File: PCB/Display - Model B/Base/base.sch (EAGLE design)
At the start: 32 parts, among them J1 SNG-2MM-HEADER-07-V, Q1 MMBT3904, Q2 MMBT3904, Q3 MMBT3904, Q4 MMBT3904, U1 PCA9634PW, U2 TSL2561FN, X1 CLOCK_LED_SEGMENT, X2 CLOCK_LED_SEGMENT, X3 CLOCK_LED_SEGMENT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

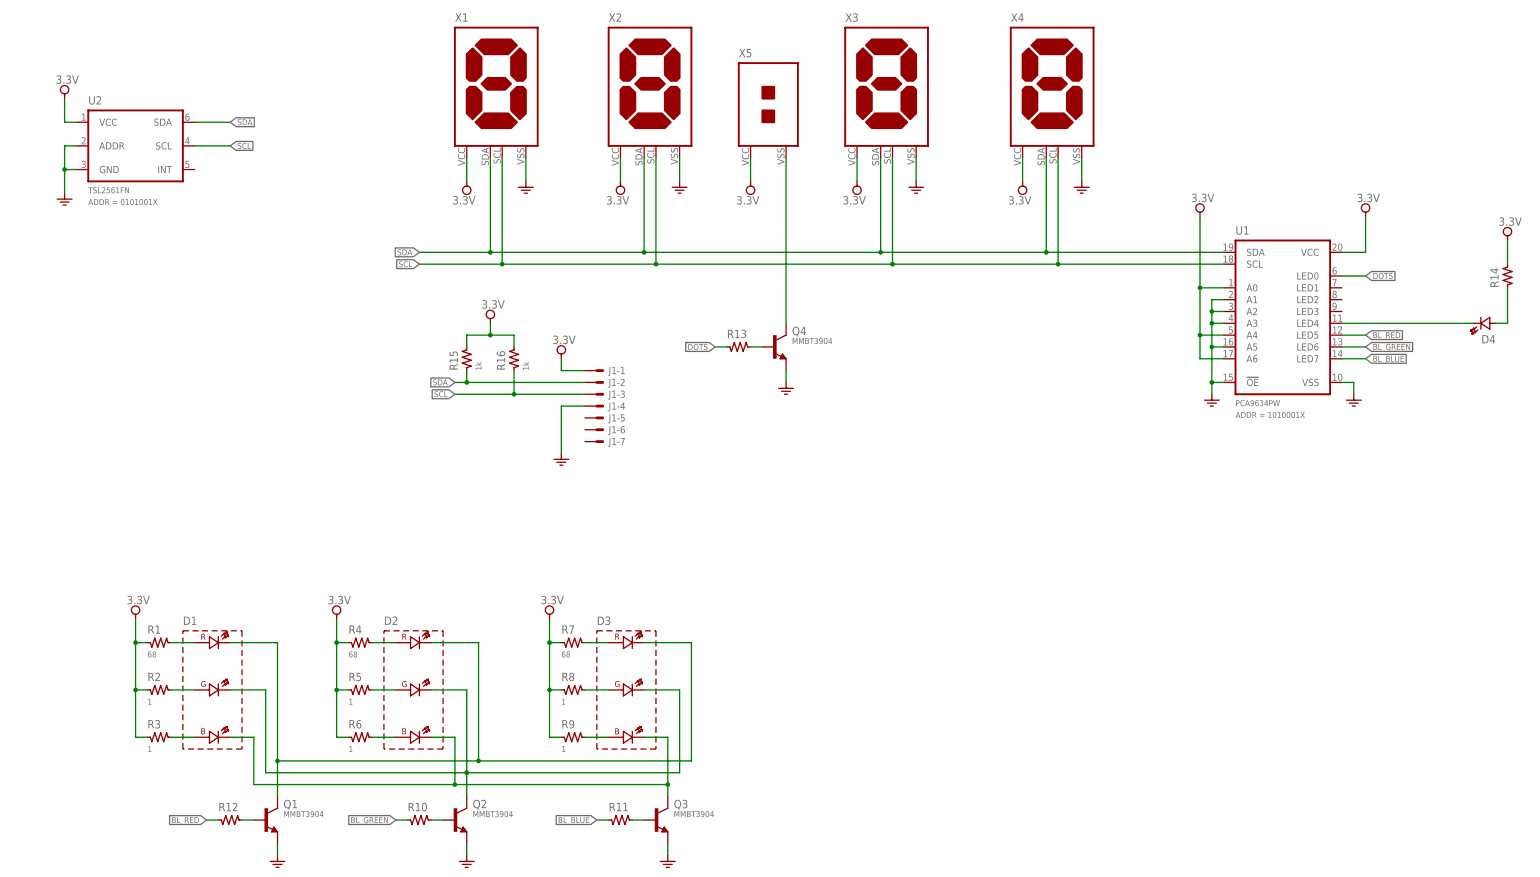
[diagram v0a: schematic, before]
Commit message: Added decoupling caps
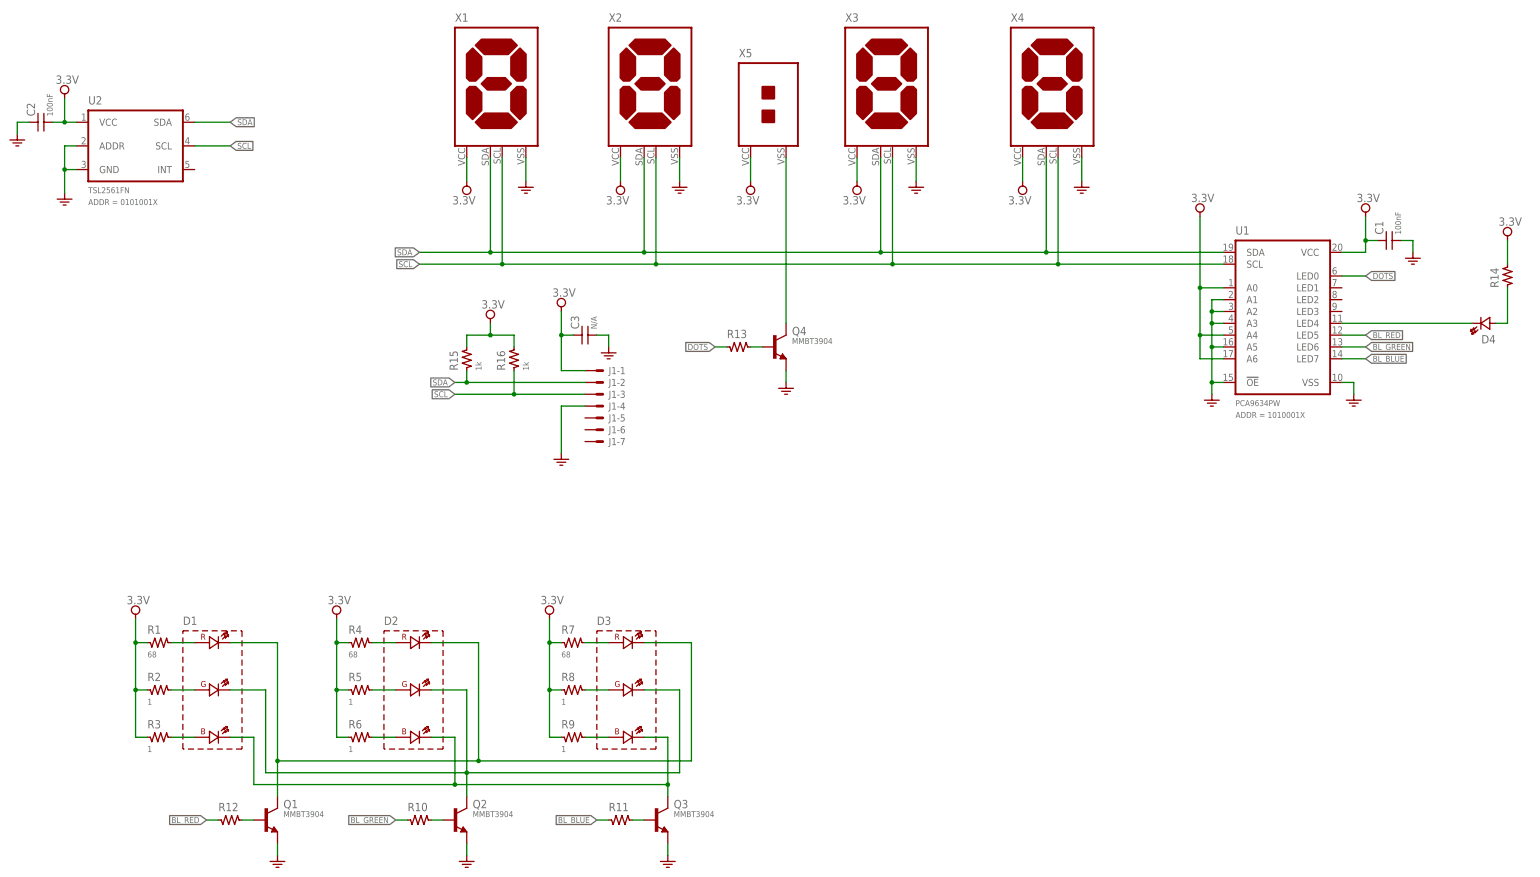
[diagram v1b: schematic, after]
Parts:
- added C1, C2: 100nF, Passive:CAP-0603
- added C3: N/A, Passive:CAP-0805
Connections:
- net 3.3V: now also C1.1, C2.2, C3.1
- net GND: now also C1.2, C2.1, C3.2
